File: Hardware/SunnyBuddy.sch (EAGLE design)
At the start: 29 parts, among them J1 5.5x2.1mm Barrel, J3 POWER_JACKPTH, J5 M02PTH, J6 M023.5MM, J7 M023.5MM, J8 M023.5MM, U1 LT3652

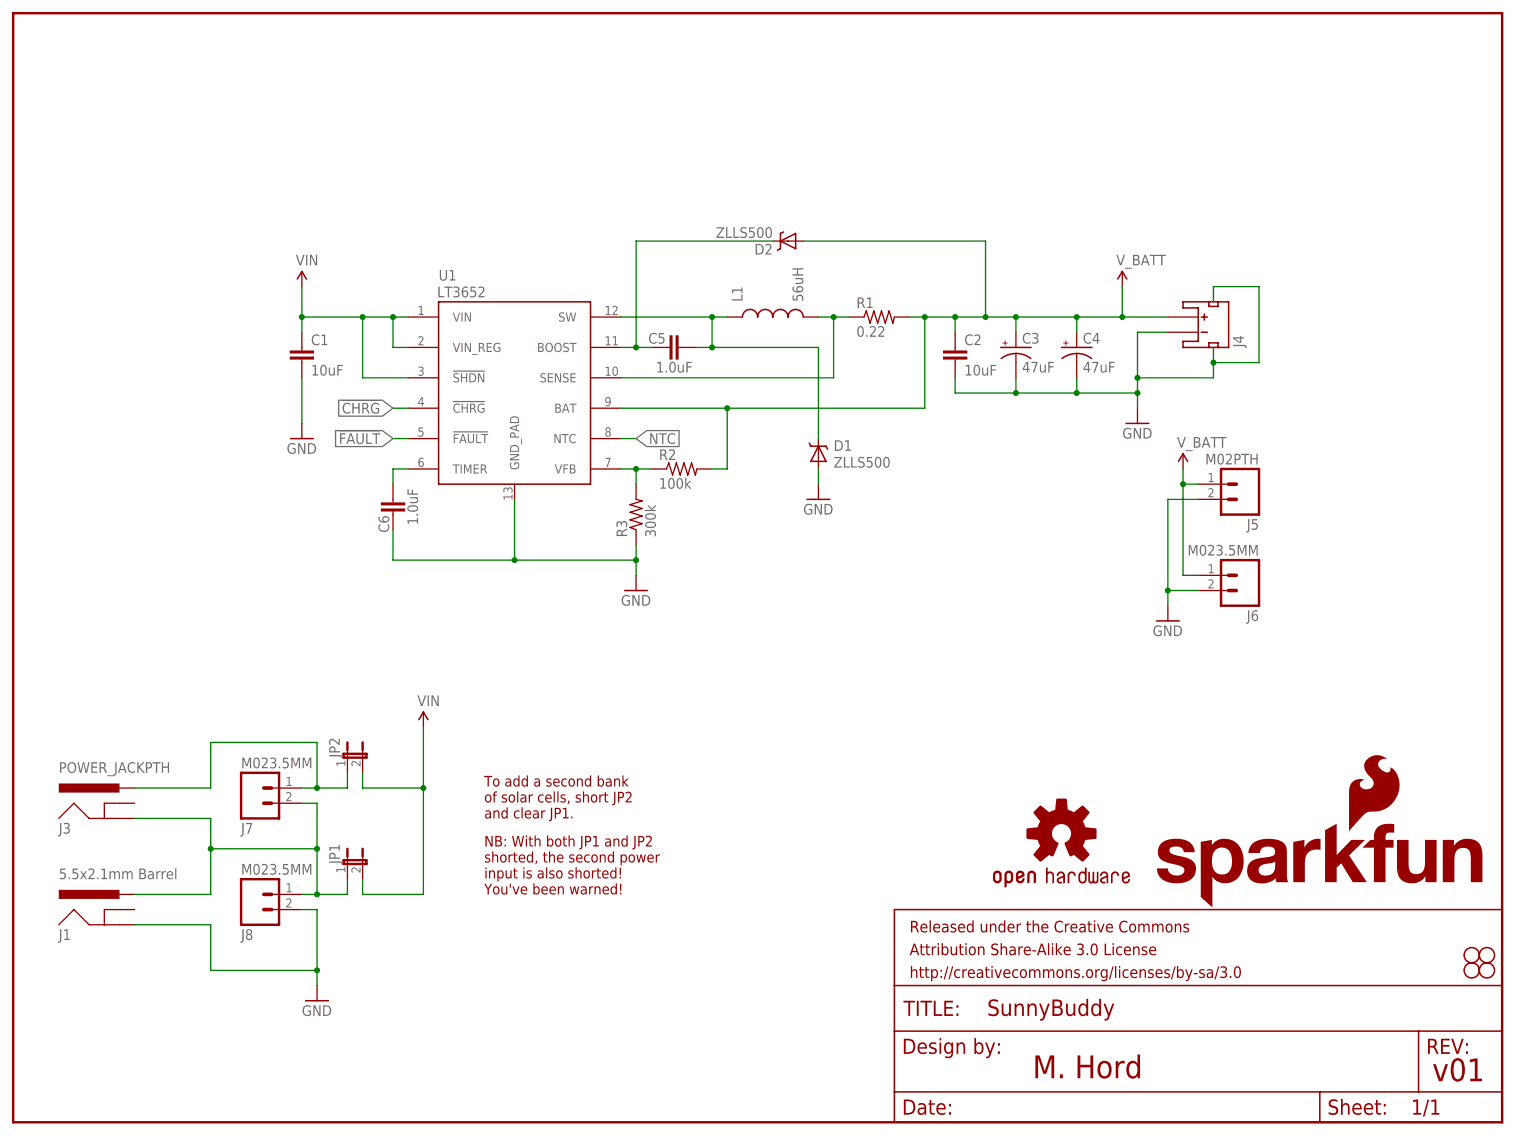
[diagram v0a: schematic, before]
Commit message: New inductor, better fb, add CHG and FLT
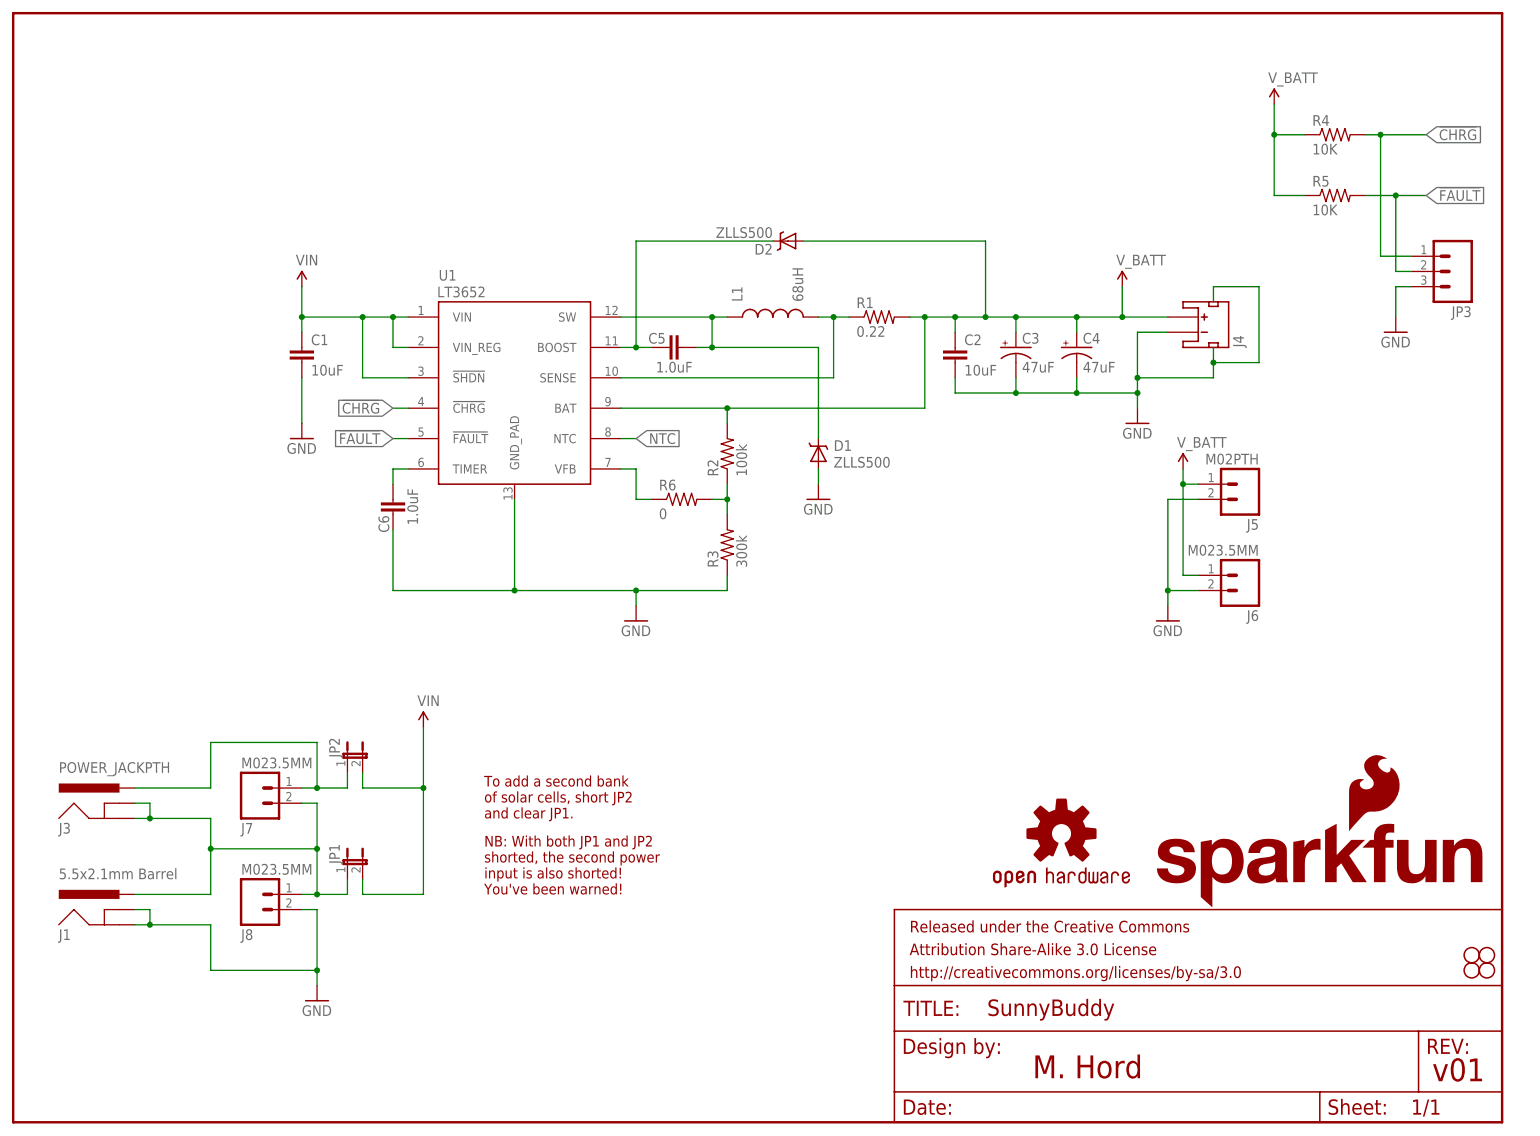
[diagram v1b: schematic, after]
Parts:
- added JP3: (no value), SparkFun-Connectors:M03PTH
- added R4, R5: 10K, SparkFun-Resistors:10KOHM1/10W1%(0603)0603
- added R6: 0, SparkFun-Resistors:0OHM1/10W5%(0603)
- L1: value 56uH -> 68uH; device SparkFun-Passives:INDUCTORSDR0403-560KL -> SparkFun-Passives:INDUCTOR68UH-1A
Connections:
- new net N$3: R6.1, U1.VFB
- net !CHRG: now also JP3.1, R4.2
- net !FAULT: now also JP3.2, R5.2
- net FB: now also R6.2; no longer U1.VFB
- net GND: now also J1.GNDBREAK, JP3.3
- net N$8: now also J3.GNDBREAK
- net V_BATT: now also R4.1, R5.1
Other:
- moved on the sheet: R2, R3
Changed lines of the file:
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@@
 <part name="C4" library="SparkFun-Capacitors" deviceset="47UF-TANT" device="" value="47uF"/>
 <part name="C2" library="SparkFun-Capacitors" deviceset="10UF-6.3V-20%(1206)" device="" value="10uF"/>
-<part name="L1" library="SparkFun-Passives" deviceset="INDUCTOR" device="SDR0403-560KL" value="56uH"/>
+<part name="L1" library="SparkFun-Passives" deviceset="INDUCTOR" device="68UH-1A" value="68uH"/>
 <part name="D1" library="SparkFun-DiscreteSemi" deviceset="ZLLS500" device="ZLLS500" value="ZLLS500"/>
 <part name="D2" library="SparkFun-DiscreteSemi" deviceset="ZLLS500" device="ZLLS500" value="ZLLS500"/>
@@
 <part name="STANDOFF3" library="SparkFun-Electromechanical" deviceset="STAND-OFF" device=""/>
 <part name="STANDOFF4" library="SparkFun-Electromechanical" deviceset="STAND-OFF" device=""/>
+<part name="R4" library="SparkFun-Resistors" deviceset="10KOHM1/10W1%(0603)" device="0603" value="10K"/>
+<part name="R5" library="SparkFun-Resistors" deviceset="10KOHM1/10W1%(0603)" device="0603" value="10K"/>
+<part name="SUPPLY5" library="SparkFun-Aesthetics" deviceset="V_BATT" device=""/>
+<part name="JP3" library="SparkFun-Connectors" deviceset="M03" device="PTH"/>
+<part name="GND7" library="SparkFun-Aesthetics" deviceset="GND" device=""/>
+<part name="R6" library="SparkFun-Resistors" deviceset="0OHM1/10W5%(0603)" device="" value="0"/>
 </parts>
 <sheets>
@@
 <attribute name="VALUE" x="67.691" y="99.822" size="1.778" layer="96" rot="R90"/>
 </instance>
-<instance part="GND4" gate="1" x="104.14" y="88.9"/>
-<instance part="R3" gate="G$1" x="104.14" y="101.6" rot="R90"/>
-<instance part="R2" gate="G$1" x="111.76" y="109.22"/>
+<instance part="GND4" gate="1" x="104.14" y="83.82"/>
+<instance part="R3" gate="G$1" x="119.38" y="96.52" rot="R90"/>
+<instance part="R2" gate="G$1" x="119.38" y="111.76" rot="R90"/>
 <instance part="J5" gate="G$1" x="205.74" y="106.68" rot="R180"/>
 <instance part="J6" gate="G$1" x="205.74" y="91.44" rot="R180"/>
@@
 <instance part="STANDOFF3" gate="G$1" x="243.84" y="27.94"/>
 <instance part="STANDOFF4" gate="G$1" x="243.84" y="25.4"/>
+<instance part="R4" gate="G$1" x="220.98" y="165.1"/>
+<instance part="R5" gate="G$1" x="220.98" y="154.94"/>
+<instance part="SUPPLY5" gate="G$1" x="210.82" y="170.18"/>
+<instance part="JP3" gate="G$1" x="241.3" y="142.24" rot="R180"/>
+<instance part="GND7" gate="1" x="231.14" y="132.08"/>
+<instance part="R6" gate="G$1" x="111.76" y="104.14"/>
 </instances>
 <busses>
@@
 <pinref part="U1" gate="G$1" pin="GND_PAD"/>
 <pinref part="C6" gate="G$1" pin="1"/>
-<wire x1="83.82" y1="93.98" x2="83.82" y2="104.14" width="0.1524" layer="91"/>
-<wire x1="63.5" y1="99.06" x2="63.5" y2="93.98" width="0.1524" layer="91"/>
-<wire x1="63.5" y1="93.98" x2="83.82" y2="93.98" width="0.1524" layer="91"/>
-<junction x="83.82" y="93.98"/>
+<wire x1="83.82" y1="88.9" x2="83.82" y2="104.14" width="0.1524" layer="91"/>
+<wire x1="63.5" y1="99.06" x2="63.5" y2="88.9" width="0.1524" layer="91"/>
+<wire x1="63.5" y1="88.9" x2="83.82" y2="88.9" width="0.1524" layer="91"/>
+<junction x="83.82" y="88.9"/>
 <pinref part="R3" gate="G$1" pin="1"/>
-<wire x1="104.14" y1="96.52" x2="104.14" y2="93.98" width="0.1524" layer="91"/>
-<wire x1="104.14" y1="93.98" x2="83.82" y2="93.98" width="0.1524" layer="91"/>
+<wire x1="119.38" y1="91.44" x2="119.38" y2="88.9" width="0.1524" layer="91"/>
+<wire x1="119.38" y1="88.9" x2="104.14" y2="88.9" width="0.1524" layer="91"/>
+<wire x1="104.14" y1="88.9" x2="83.82" y2="88.9" width="0.1524" layer="91"/>
 <pinref part="GND4" gate="1" pin="GND"/>
-<wire x1="104.14" y1="91.44" x2="104.14" y2="93.98" width="0.1524" layer="91"/>
-<junction x="104.14" y="93.98"/>
+<wire x1="104.14" y1="86.36" x2="104.14" y2="88.9" width="0.1524" layer="91"/>
+<junction x="104.14" y="88.9"/>
 </segment>
 <segment>
@@
 <segment>
 <pinref part="J1" gate="G$1" pin="GND"/>
-<wire x1="20.32" y1="33.02" x2="33.02" y2="33.02" width="0.1524" layer="91"/>
+<wire x1="20.32" y1="33.02" x2="22.86" y2="33.02" width="0.1524" layer="91"/>
+<wire x1="22.86" y1="33.02" x2="33.02" y2="33.02" width="0.1524" layer="91"/>
 <wire x1="33.02" y1="33.02" x2="33.02" y2="25.4" width="0.1524" layer="91"/>
 <wire x1="33.02" y1="25.4" x2="50.8" y2="25.4" width="0.1524" layer="91"/>
@@
 <pinref part="J8" gate="G$1" pin="2"/>
 <wire x1="48.26" y1="35.56" x2="50.8" y2="35.56" width="0.1524" layer="91"/>
+<pinref part="J1" gate="G$1" pin="GNDBREAK"/>
+<wire x1="20.32" y1="35.56" x2="22.86" y2="35.56" width="0.1524" layer="91"/>
+<wire x1="22.86" y1="35.56" x2="22.86" y2="33.02" width="0.1524" layer="91"/>
+<junction x="22.86" y="33.02"/>
+</segment>
+<segment>
+<pinref part="GND7" gate="1" pin="GND"/>
+<wire x1="231.14" y1="134.62" x2="231.14" y2="139.7" width="0.1524" layer="91"/>
+<pinref part="JP3" gate="G$1" pin="3"/>
+<wire x1="231.14" y1="139.7" x2="233.68" y2="139.7" width="0.1524" layer="91"/>
 </segment>
 </net>
@@
 <net name="FB" class="0">
 <segment>
-<pinref part="U1" gate="G$1" pin="VFB"/>
 <pinref part="R2" gate="G$1" pin="1"/>
-<wire x1="101.6" y1="109.22" x2="104.14" y2="109.22" width="0.1524" layer="91"/>
 <pinref part="R3" gate="G$1" pin="2"/>
-<wire x1="104.14" y1="109.22" x2="106.68" y2="109.22" width="0.1524" layer="91"/>
-<wire x1="104.14" y1="109.22" x2="104.14" y2="106.68" width="0.1524" layer="91"/>
-<junction x="104.14" y="109.22"/>
+<wire x1="119.38" y1="101.6" x2="119.38" y2="104.14" width="0.1524" layer="91"/>
+<pinref part="R6" gate="G$1" pin="2"/>
+<wire x1="119.38" y1="104.14" x2="119.38" y2="106.68" width="0.1524" layer="91"/>
+<wire x1="116.84" y1="104.14" x2="119.38" y2="104.14" width="0.1524" layer="91"/>
+<junction x="119.38" y="104.14"/>
 </segment>
 </net>
@@
 <label x="63.5" y="119.38" size="1.778" layer="95" rot="R180" xref="yes"/>
 </segment>
+<segment>
+<pinref part="R4" gate="G$1" pin="2"/>
+<wire x1="226.06" y1="165.1" x2="228.6" y2="165.1" width="0.1524" layer="91"/>
+<label x="236.22" y="165.1" size="1.778" layer="95" xref="yes"/>
+<wire x1="228.6" y1="165.1" x2="236.22" y2="165.1" width="0.1524" layer="91"/>
+<wire x1="228.6" y1="165.1" x2="228.6" y2="144.78" width="0.1524" layer="91"/>
+<junction x="228.6" y="165.1"/>
+<pinref part="JP3" gate="G$1" pin="1"/>
+<wire x1="228.6" y1="144.78" x2="233.68" y2="144.78" width="0.1524" layer="91"/>
+</segment>
 </net>
 <net name="!FAULT" class="0">
@@
 <wire x1="66.04" y1="114.3" x2="63.5" y2="114.3" width="0.1524" layer="91"/>
 <label x="63.5" y="114.3" size="1.778" layer="95" rot="R180" xref="yes"/>
+</segment>
+<segment>
+<pinref part="R5" gate="G$1" pin="2"/>
+<wire x1="226.06" y1="154.94" x2="231.14" y2="154.94" width="0.1524" layer="91"/>
+<label x="236.22" y="154.94" size="1.778" layer="95" xref="yes"/>
+<wire x1="231.14" y1="154.94" x2="236.22" y2="154.94" width="0.1524" layer="91"/>
+<wire x1="231.14" y1="154.94" x2="231.14" y2="142.24" width="0.1524" layer="91"/>
+<junction x="231.14" y="154.94"/>
+<pinref part="JP3" gate="G$1" pin="2"/>
+<wire x1="231.14" y1="142.24" x2="233.68" y2="142.24" width="0.1524" layer="91"/>
 </segment>
 </net>
@@
 <pinref part="R2" gate="G$1" pin="2"/>
 <wire x1="185.42" y1="134.62" x2="193.04" y2="134.62" width="0.1524" layer="91"/>
-<wire x1="116.84" y1="109.22" x2="119.38" y2="109.22" width="0.1524" layer="91"/>
-<wire x1="119.38" y1="109.22" x2="119.38" y2="119.38" width="0.1524" layer="91"/>
+<wire x1="119.38" y1="116.84" x2="119.38" y2="119.38" width="0.1524" layer="91"/>
 <junction x="119.38" y="119.38"/>
 <pinref part="SUPPLY1" gate="G$1" pin="V_BATT"/>
@@
 <wire x1="195.58" y1="91.44" x2="198.12" y2="91.44" width="0.1524" layer="91"/>
 </segment>
+<segment>
+<pinref part="SUPPLY5" gate="G$1" pin="V_BATT"/>
+<wire x1="210.82" y1="170.18" x2="210.82" y2="165.1" width="0.1524" layer="91"/>
+<pinref part="R4" gate="G$1" pin="1"/>
+<wire x1="210.82" y1="165.1" x2="215.9" y2="165.1" width="0.1524" layer="91"/>
+<wire x1="210.82" y1="165.1" x2="210.82" y2="154.94" width="0.1524" layer="91"/>
+<junction x="210.82" y="165.1"/>
+<pinref part="R5" gate="G$1" pin="1"/>
+<wire x1="210.82" y1="154.94" x2="215.9" y2="154.94" width="0.1524" layer="91"/>
+</segment>
 </net>
 <net name="N$8" class="0">
 <segment>
 <pinref part="J3" gate="G$1" pin="GND"/>
-<wire x1="20.32" y1="50.8" x2="33.02" y2="50.8" width="0.1524" layer="91"/>
+<wire x1="20.32" y1="50.8" x2="22.86" y2="50.8" width="0.1524" layer="91"/>
+<wire x1="22.86" y1="50.8" x2="33.02" y2="50.8" width="0.1524" layer="91"/>
 <wire x1="33.02" y1="50.8" x2="33.02" y2="45.72" width="0.1524" layer="91"/>
 <pinref part="J1" gate="G$1" pin="PWR"/>
@@
 <junction x="50.8" y="45.72"/>
 <junction x="50.8" y="38.1"/>
+<pinref part="J3" gate="G$1" pin="GNDBREAK"/>
+<wire x1="20.32" y1="53.34" x2="22.86" y2="53.34" width="0.1524" layer="91"/>
+<wire x1="22.86" y1="53.34" x2="22.86" y2="50.8" width="0.1524" layer="91"/>
+<junction x="22.86" y="50.8"/>
 </segment>
 </net>
@@
 </segment>
 </net>
+<net name="N$3" class="0">
+<segment>
+<pinref part="R6" gate="G$1" pin="1"/>
+<wire x1="106.68" y1="104.14" x2="104.14" y2="104.14" width="0.1524" layer="91"/>
+<wire x1="104.14" y1="104.14" x2="104.14" y2="109.22" width="0.1524" layer="91"/>
+<pinref part="U1" gate="G$1" pin="VFB"/>
+<wire x1="104.14" y1="109.22" x2="101.6" y2="109.22" width="0.1524" layer="91"/>
+</segment>
+</net>

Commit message: Change version numbers
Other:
- note added: "v02"
- note removed: "v01"
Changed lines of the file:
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@@
 input is also shorted!
 You've been warned!</text>
-<text x="237.236" y="6.858" size="3.81" layer="94">v01</text>
+<text x="237.236" y="6.858" size="3.81" layer="94">v02</text>
 <text x="170.434" y="7.366" size="3.81" layer="94">M. Hord</text>
 </plain>

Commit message: Release to reds, chg v#, move 1 via, add pol silk
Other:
- note added: "v10"
- note removed: "v02"
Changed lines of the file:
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@@
 input is also shorted!
 You've been warned!</text>
-<text x="237.236" y="6.858" size="3.81" layer="94">v02</text>
+<text x="237.236" y="6.858" size="3.81" layer="94">v10</text>
 <text x="170.434" y="7.366" size="3.81" layer="94">M. Hord</text>
 </plain>
